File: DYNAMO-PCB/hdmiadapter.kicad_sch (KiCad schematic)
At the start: 1 part, among them U2 CH7035B-BF

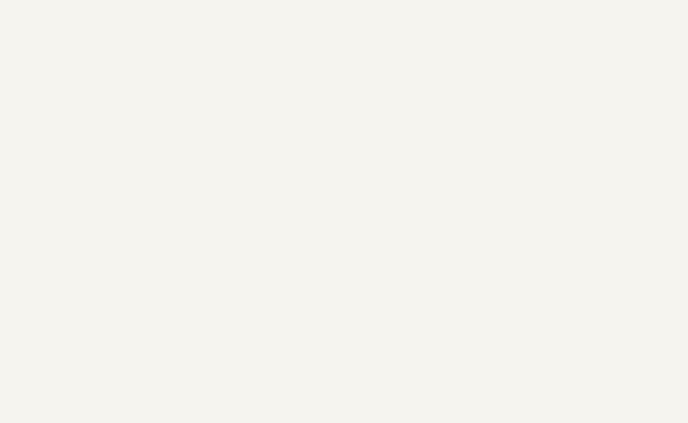
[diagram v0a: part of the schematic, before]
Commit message: second hdmi port on subsheet
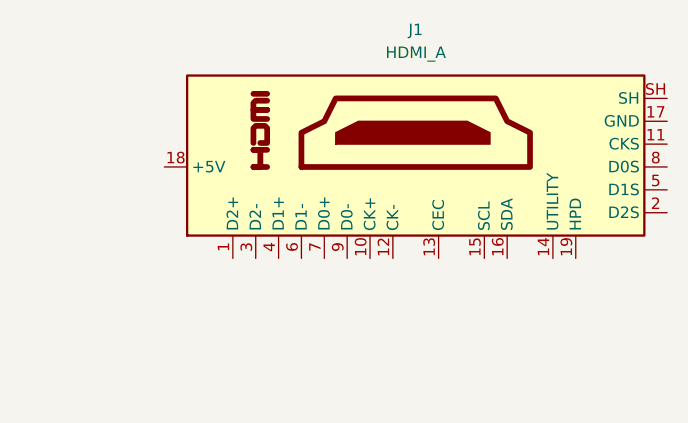
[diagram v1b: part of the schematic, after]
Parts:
- added J1: HDMI_A, Connector_Video:HDMI_A_Molex_208658-1001_Horizontal, symbol Connector:HDMI_A
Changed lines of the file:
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@@
+		)
+	)
+	(symbol
+		(lib_id "Connector:HDMI_A")
+		(at 229.87 39.37 90)
+		(unit 1)
+		(exclude_from_sim no)
+		(in_bom yes)
+		(on_board yes)
+		(dnp no)
+		(fields_autoplaced yes)
+		(property "Reference" "J1"
+			(at 229.87 24.13 90)
+			(effects
+				(font
+					(size 1.27 1.27)
+				)
+			)
+		)
+		(property "Value" "HDMI_A"
+			(at 229.87 26.67 90)
+			(effects
+				(font
+					(size 1.27 1.27)
+				)
+			)
+		)
+		(property "Footprint" "Connector_Video:HDMI_A_Molex_208658-1001_Horizontal"
+			(at 229.87 38.735 0)
+			(effects
+				(font
+					(size 1.27 1.27)
+				)
+				(hide yes)
+			)
+		)
+		(property "Datasheet" "https://en.wikipedia.org/wiki/HDMI"
+			(at 229.87 38.735 0)
+			(effects
+				(font
+					(size 1.27 1.27)
+				)
+				(hide yes)
+			)
+		)
+		(property "Description" "HDMI type A connector"
+			(at 229.87 39.37 0)
+			(effects
+				(font
+					(size 1.27 1.27)
+				)
+				(hide yes)
+			)
+		)
+		(pin "6"
+		)
+		(pin "9"
+		)
+		(pin "12"
+		)
+		(pin "16"
+		)
+		(pin "14"
+		)
+		(pin "19"
+		)
+		(pin "1"
+		)
+		(pin "3"
+		)
+		(pin "4"
+		)
+		(pin "7"
+		)
+		(pin "10"
+		)
+		(pin "13"
+		)
+		(pin "15"
+		)
+		(pin "17"
+		)
+		(pin "5"
+		)
+		(pin "8"
+		)
+		(pin "18"
+		)
+		(pin "2"
+		)
+		(pin "11"
+		)
+		(pin "SH"
+		)
+		(instances
+			(project "DYNAMO-PCB"
+				(path "/2ca9dd43-411d-4cc5-8a4b-ed00d72bae91/40ca106a-4397-464b-b6b2-602763c1b463"
+					(reference "J1")
+					(unit 1)
+				)
+			)
 		)
 	)

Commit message: schematic wip
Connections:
- net at U2.31 (~{TLC}): now also J1.12 (CK-)
- net at U2.32 (TLC): now also J1.10 (CK+)
- net at U2.34 (~{TDC0}): now also J1.9 (D0-)
- net at U2.35 (TDC0): now also J1.7 (D0+)
- net at U2.36 (~{TDC1}): now also J1.6 (D1-)
- net at U2.37 (TDC1): now also J1.4 (D1+)
- net at U2.39 (~{TDC2}): now also J1.3 (D2-)
- net at U2.40 (TDC2): now also J1.1 (D2+)
- net at U2.51 (HPD): now also J1.19 (HPD)
- net at U2.64 (DDC_SD): now also J1.16 (SDA)
- net GND: now reaches J1.11 (CKS)
- net GND: now also J1.17 (GND), J1.2 (D2S), J1.5 (D1S), J1.8 (D0S), J1.SH
- no-connect marks 0 -> 3
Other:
- moved on the sheet: J1

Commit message: schematic wip
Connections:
- net at U2.63 (DDC_SC): now also J1.15 (SCL)
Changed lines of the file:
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@@
+	(wire
+		(pts
+			(xy 170.18 92.71) (xy 213.36 92.71)
+		)
+		(stroke
+			(width 0)
+			(type default)
+		)
+	)
 	(wire
 		(pts
@@
 	(wire
 		(pts
-			(xy 214.63 49.53) (xy 214.63 90.17)
+			(xy 214.63 49.53) (xy 214.63 91.44)
 		)
 		(stroke
@@
 		)
 		(stroke
+			(width 0)
+			(type default)
+		)
+	)
+	(wire
+		(pts
+			(xy 214.63 91.44) (xy 213.36 92.71)
+		)
+		(stroke
